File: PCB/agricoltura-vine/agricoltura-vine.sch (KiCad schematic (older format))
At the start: 0 parts

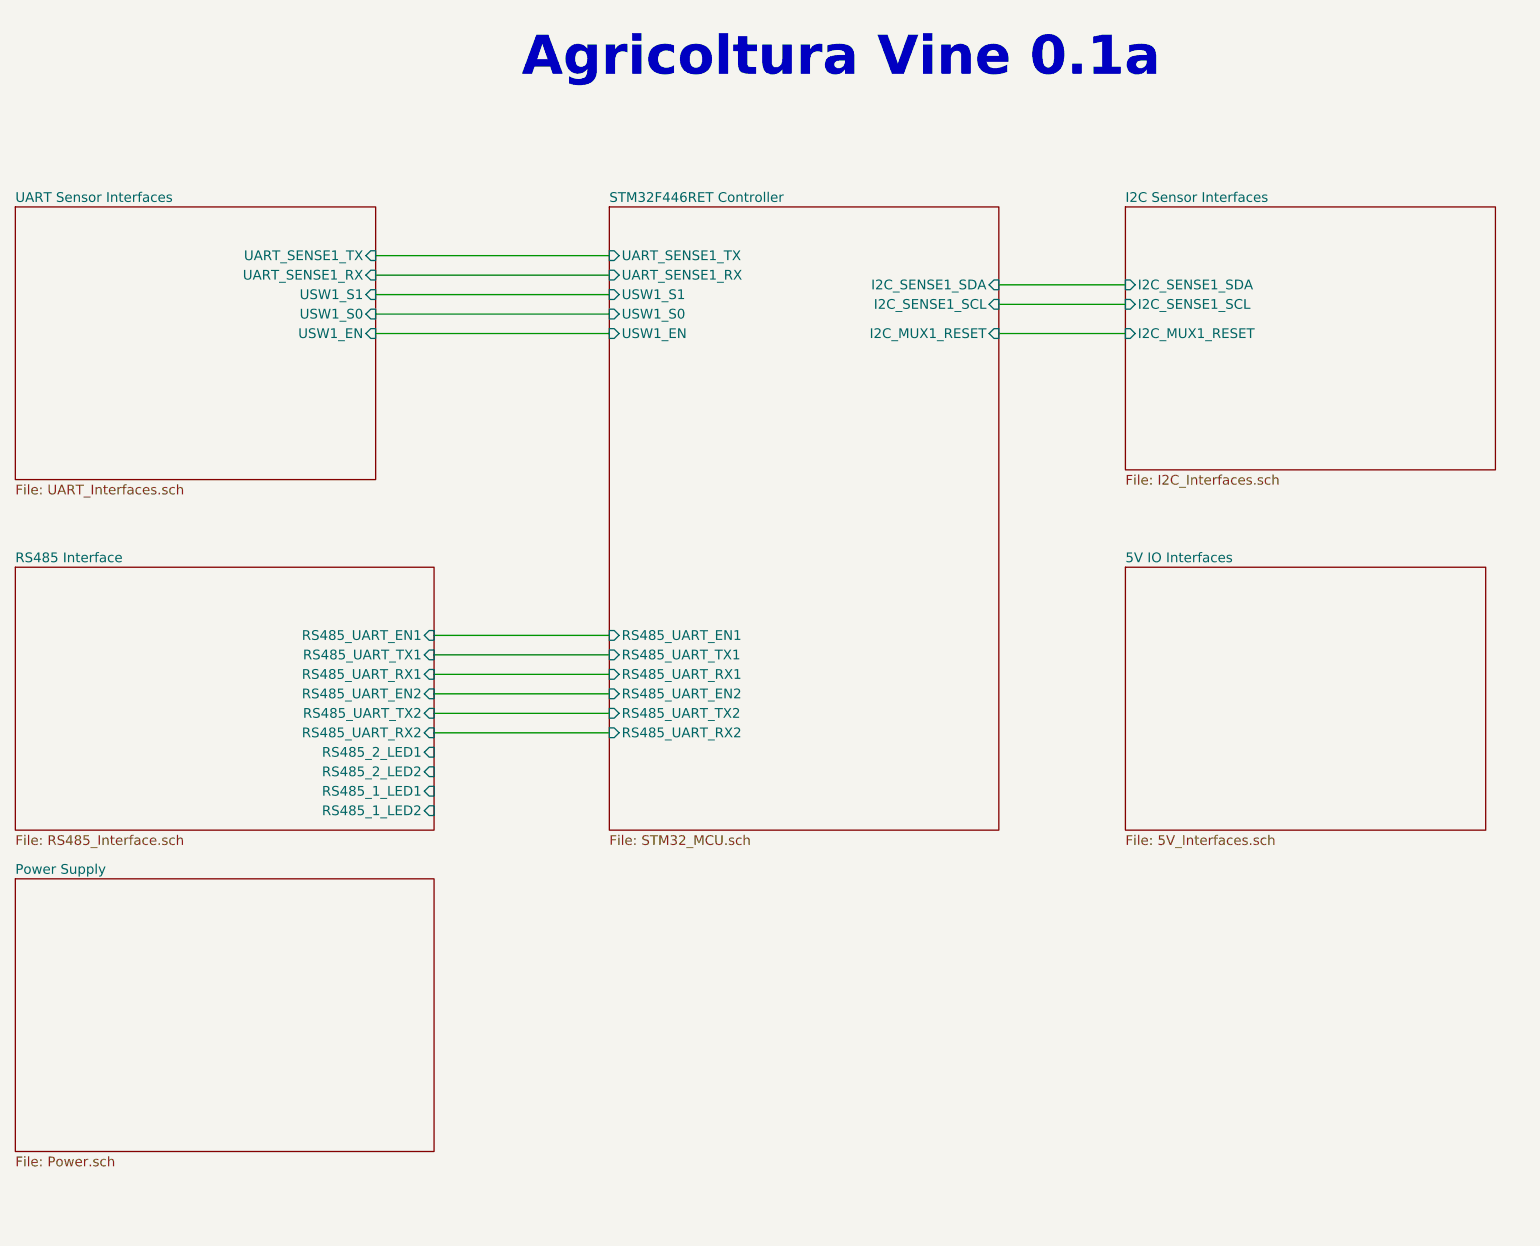
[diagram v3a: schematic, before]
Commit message: Routing and New RS485
swapped over the RS485 chip to a new one and started routing the board.
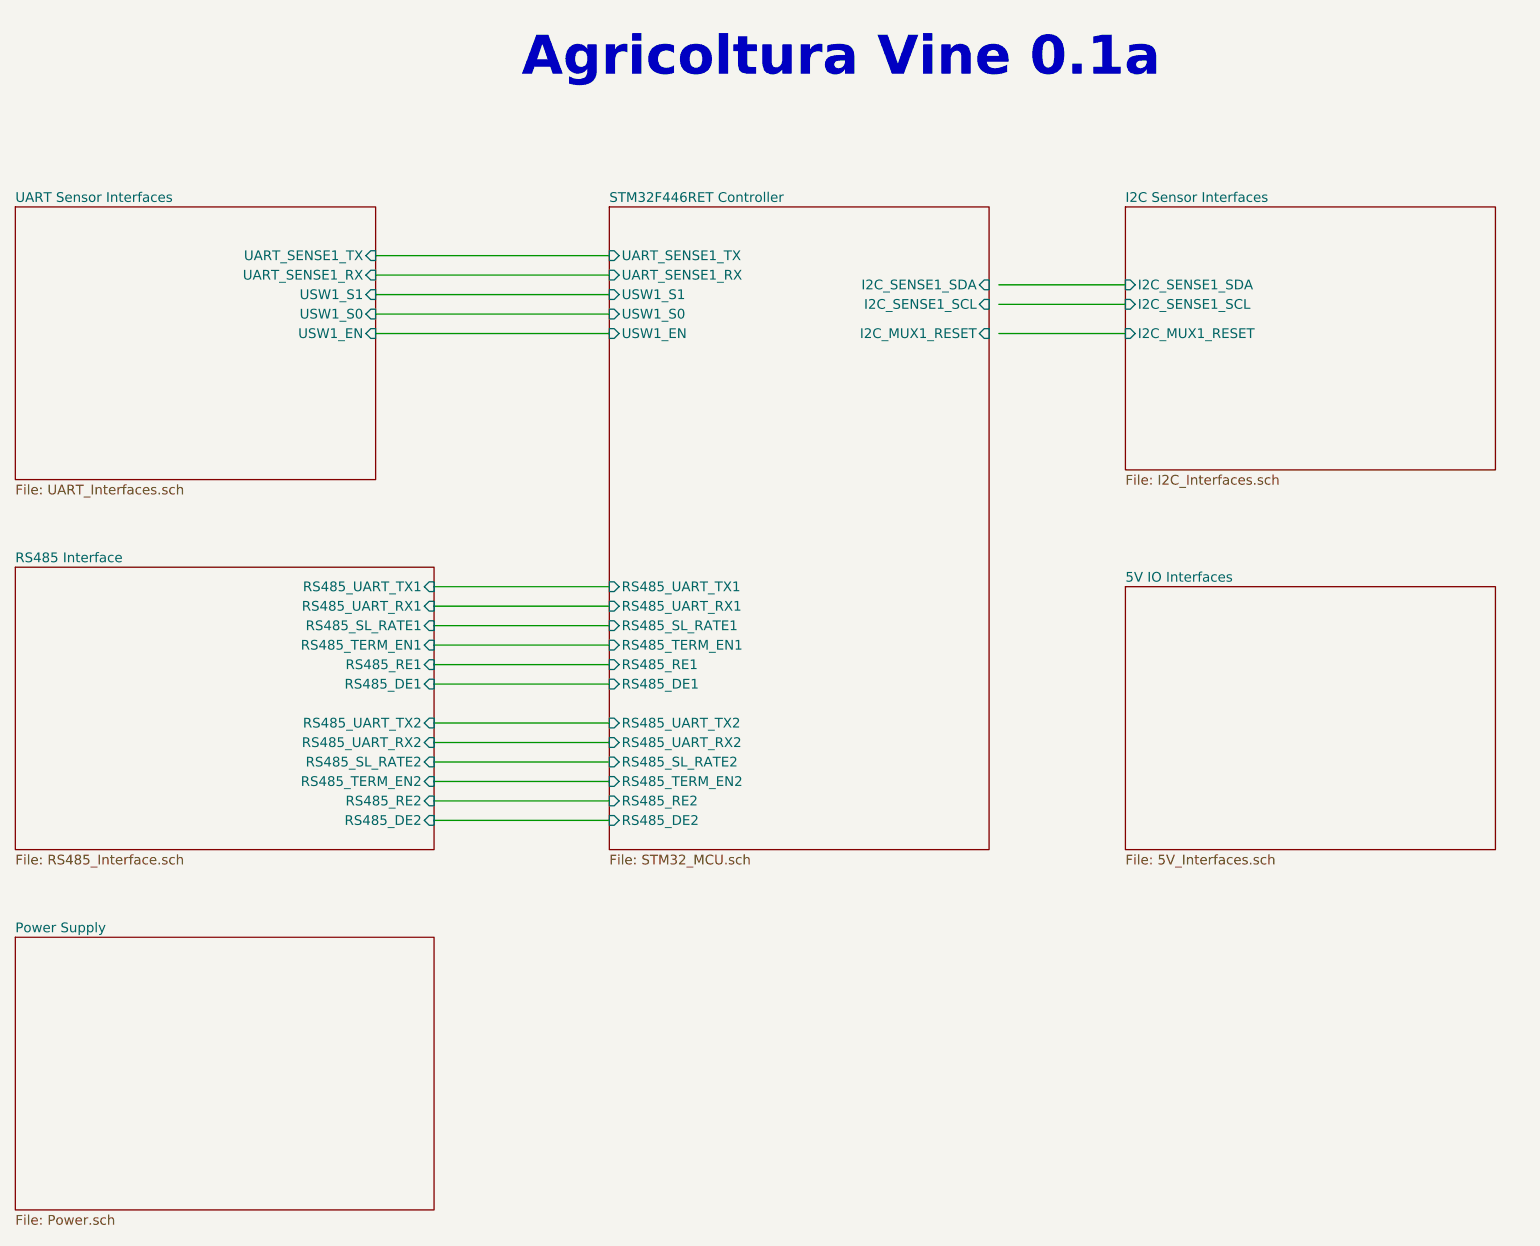
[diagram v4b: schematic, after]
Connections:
- wire segments 14 -> 20
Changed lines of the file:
@@
 $EndDescr
 $Sheet
-S 4700 2000 2000 3200
+S 4700 2000 1950 3300
 U 5EE8264D
 F0 "STM32F446RET Controller" 50
 F1 "STM32_MCU.sch" 50
 F2 "UART_SENSE1_TX" I L 4700 2250 50
-F3 "RS485_UART_EN1" I L 4700 4200 50
-F4 "RS485_UART_TX1" I L 4700 4300 50
-F5 "RS485_UART_RX1" I L 4700 4400 50
-F6 "RS485_UART_EN2" I L 4700 4500 50
-F7 "RS485_UART_TX2" I L 4700 4600 50
-F8 "RS485_UART_RX2" I L 4700 4700 50
-F9 "I2C_SENSE1_SDA" I R 6700 2400 50
-F10 "I2C_SENSE1_SCL" I R 6700 2500 50
-F11 "I2C_MUX1_RESET" I R 6700 2650 50
-F12 "USW1_EN" I L 4700 2650 50
-F13 "USW1_S0" I L 4700 2550 50
-F14 "USW1_S1" I L 4700 2450 50
-F15 "UART_SENSE1_RX" I L 4700 2350 50
+F3 "RS485_UART_TX1" I L 4700 3950 50
+F4 "RS485_UART_RX1" I L 4700 4050 50
+F5 "RS485_UART_TX2" I L 4700 4650 50
+F6 "RS485_UART_RX2" I L 4700 4750 50
+F7 "I2C_SENSE1_SDA" I R 6650 2400 50
+F8 "I2C_SENSE1_SCL" I R 6650 2500 50
+F9 "I2C_MUX1_RESET" I R 6650 2650 50
+F10 "USW1_EN" I L 4700 2650 50
+F11 "USW1_S0" I L 4700 2550 50
+F12 "USW1_S1" I L 4700 2450 50
+F13 "UART_SENSE1_RX" I L 4700 2350 50
+F14 "RS485_DE1" I L 4700 4450 50
+F15 "RS485_DE2" I L 4700 5150 50
+F16 "RS485_TERM_EN1" I L 4700 4250 50
+F17 "RS485_SL_RATE1" I L 4700 4150 50
+F18 "RS485_RE1" I L 4700 4350 50
+F19 "RS485_SL_RATE2" I L 4700 4850 50
+F20 "RS485_RE2" I L 4700 5050 50
+F21 "RS485_TERM_EN2" I L 4700 4950 50
 $EndSheet
 $Sheet
@@
 $EndSheet
 $Sheet
-S 1650 5450 2150 1400
+S 1650 5750 2150 1400
 U 5EE8280D
 F0 "Power Supply" 50
@@
 $EndSheet
 $Sheet
-S 1650 3850 2150 1350
+S 1650 3850 2150 1450
 U 5EE82896
 F0 "RS485 Interface" 50
 F1 "RS485_Interface.sch" 50
-F2 "RS485_UART_EN1" I R 3800 4200 50
-F3 "RS485_UART_TX1" I R 3800 4300 50
-F4 "RS485_UART_RX1" I R 3800 4400 50
-F5 "RS485_UART_EN2" I R 3800 4500 50
-F6 "RS485_UART_TX2" I R 3800 4600 50
-F7 "RS485_UART_RX2" I R 3800 4700 50
-F8 "RS485_2_LED1" I R 3800 4800 50
-F9 "RS485_2_LED2" I R 3800 4900 50
-F10 "RS485_1_LED1" I R 3800 5000 50
-F11 "RS485_1_LED2" I R 3800 5100 50
-$EndSheet
-$Sheet
-S 7350 3850 1850 1350
-U 5EF943A9
-F0 "5V IO Interfaces" 50
-F1 "5V_Interfaces.sch" 50
+F2 "RS485_UART_TX1" I R 3800 3950 50
+F3 "RS485_UART_RX1" I R 3800 4050 50
+F4 "RS485_UART_TX2" I R 3800 4650 50
+F5 "RS485_UART_RX2" I R 3800 4750 50
+F6 "RS485_DE2" I R 3800 5150 50
+F7 "RS485_DE1" I R 3800 4450 50
+F8 "RS485_SL_RATE2" I R 3800 4850 50
+F9 "RS485_SL_RATE1" I R 3800 4150 50
+F10 "RS485_TERM_EN1" I R 3800 4250 50
+F11 "RS485_RE1" I R 3800 4350 50
+F12 "RS485_RE2" I R 3800 5050 50
+F13 "RS485_TERM_EN2" I R 3800 4950 50
 $EndSheet
 Wire Wire Line
-	3800 4200 4700 4200
+	3800 3950 4700 3950
 Wire Wire Line
-	3800 4300 4700 4300
+	4700 4050 3800 4050
 Wire Wire Line
-	4700 4400 3800 4400
+	4700 4650 3800 4650
 Wire Wire Line
-	3800 4500 4700 4500
-Wire Wire Line
-	4700 4600 3800 4600
-Wire Wire Line
-	3800 4700 4700 4700
+	3800 4750 4700 4750
 Wire Wire Line
 	7350 2650 6700 2650
@@
 Text Notes 4250 1350 0    200  ~ 40
 Agricoltura Vine 0.1a
+$Sheet
+S 7350 3950 1900 1350
+U 5EF943A9
+F0 "5V IO Interfaces" 50
+F1 "5V_Interfaces.sch" 50
+$EndSheet
+Wire Wire Line
+	4700 4850 3800 4850
+Wire Wire Line
+	3800 4950 4700 4950
+Wire Wire Line
+	4700 5050 3800 5050
+Wire Wire Line
+	3800 5150 4700 5150
+Wire Wire Line
+	4700 4350 3800 4350
+Wire Wire Line
+	3800 4450 4700 4450
+Wire Wire Line
+	4700 4150 3800 4150
+Wire Wire Line
+	3800 4250 4700 4250
 $EndSCHEMATC

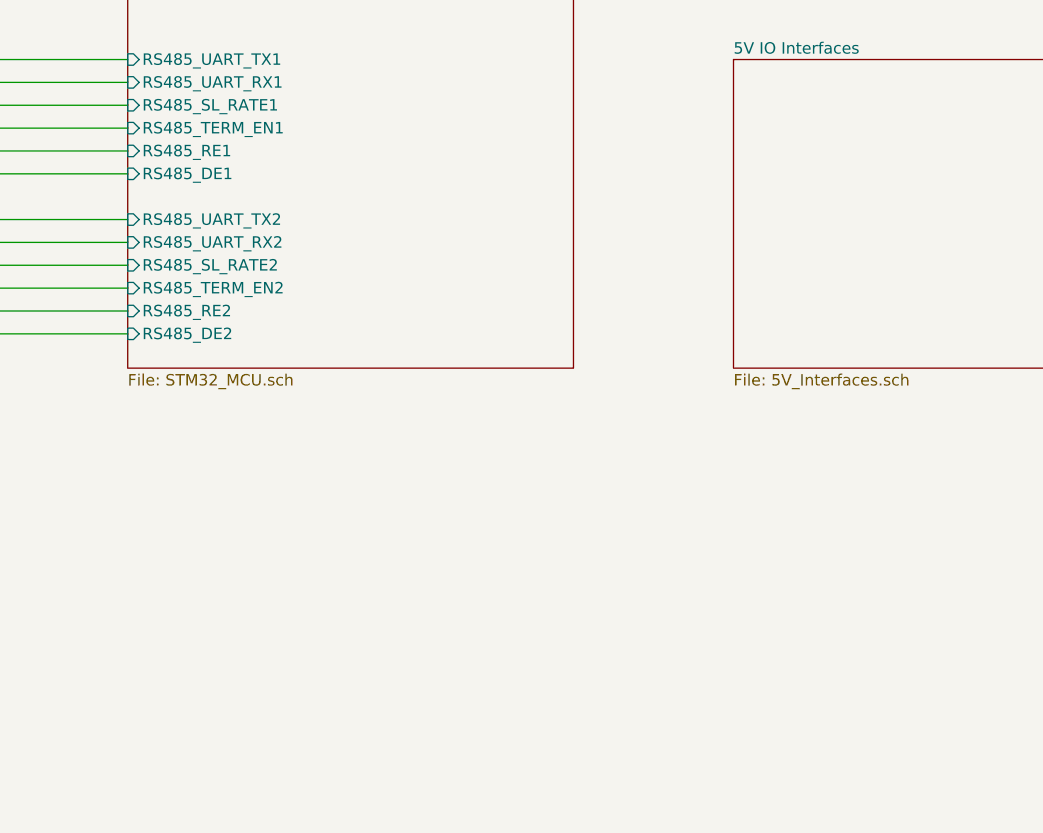
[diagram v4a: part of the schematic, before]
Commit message: Majopr Progress
Board shape enlarged to simplify layout and accomodate larger size parts for sisterboard like Ivy. QWIIC connectors flipped to be correct, signals were oriented incorrectly in past revisions.
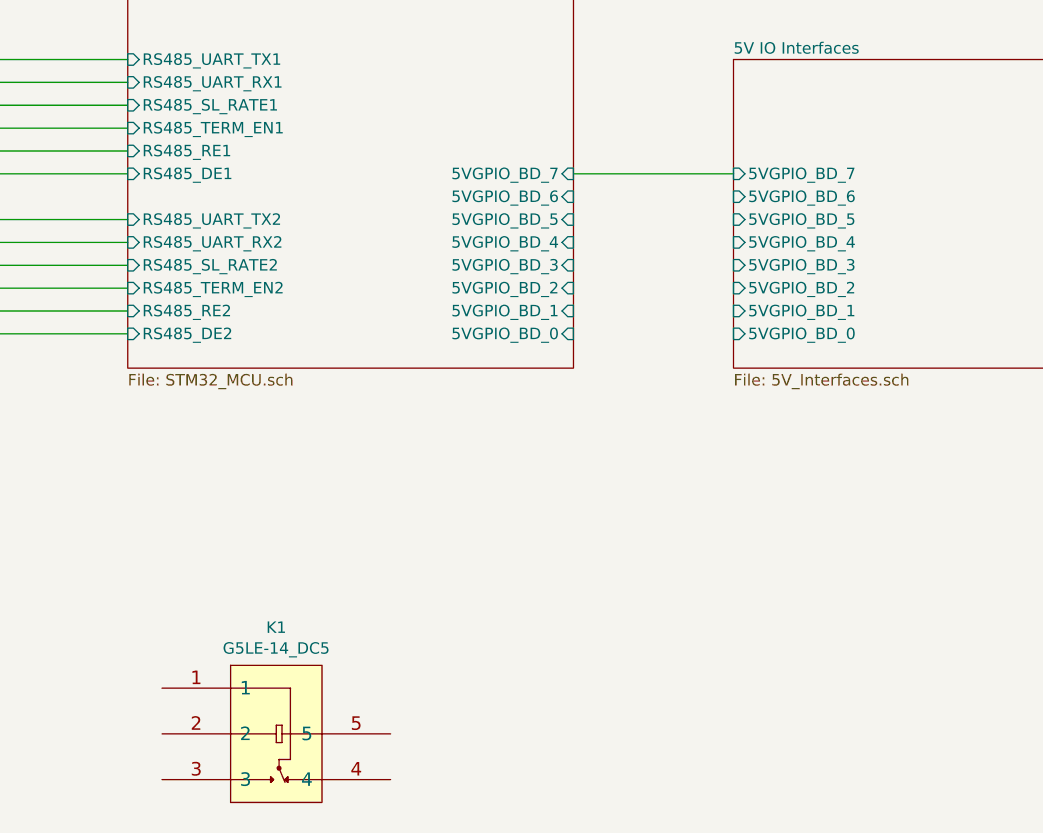
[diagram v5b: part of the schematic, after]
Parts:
- added K1: G5LE-14_DC5, AVR-KiCAD-Lib-Relays-Contactors:G5LE-14_DC5, symbol AVR-KiCAD-Lib-Mech-Relays-Contactors:G5LE-14_DC5
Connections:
- wire segments 20 -> 21
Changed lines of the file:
@@
 F20 "RS485_RE2" I L 4700 5050 50
 F21 "RS485_TERM_EN2" I L 4700 4950 50
+F22 "5VGPIO_BD_0" I R 6650 5150 50
+F23 "5VGPIO_BD_1" I R 6650 5050 50
+F24 "5VGPIO_BD_2" I R 6650 4950 50
+F25 "5VGPIO_BD_3" I R 6650 4850 50
+F26 "5VGPIO_BD_4" I R 6650 4750 50
+F27 "5VGPIO_BD_5" I R 6650 4650 50
+F28 "5VGPIO_BD_6" I R 6650 4550 50
+F29 "5VGPIO_BD_7" I R 6650 4450 50
 $EndSheet
 $Sheet
@@
 F0 "5V IO Interfaces" 50
 F1 "5V_Interfaces.sch" 50
+F2 "5VGPIO_BD_0" I L 7350 5150 50
+F3 "5VGPIO_BD_1" I L 7350 5050 50
+F4 "5VGPIO_BD_2" I L 7350 4950 50
+F5 "5VGPIO_BD_3" I L 7350 4850 50
+F6 "5VGPIO_BD_4" I L 7350 4750 50
+F7 "5VGPIO_BD_5" I L 7350 4650 50
+F8 "5VGPIO_BD_6" I L 7350 4550 50
+F9 "5VGPIO_BD_7" I L 7350 4450 50
 $EndSheet
 Wire Wire Line
@@
 Wire Wire Line
 	3800 4250 4700 4250
+Wire Wire Line
+	6650 4450 7350 4450
+$Comp
+L AVR-KiCAD-Lib-Mech-Relays-Contactors:G5LE-14_DC5 K1
+U 1 1 5F0092A7
+P 5150 6600
+F 0 "K1" H 5350 6765 50  0000 C CNN
+F 1 "G5LE-14_DC5" H 5350 6674 50  0000 C CNN
+F 2 "AVR-KiCAD-Lib-Relays-Contactors:G5LE-14_DC5" H 5150 6600 50  0001 C CNN
+F 3 "https://omronfs.omron.com/en_US/ecb/products/pdf/en-g5le.pdf" H 5150 6600 50  0001 C CNN
+F 4 "1.44000" H 5250 6850 50  0001 C CNN "Cost QTY: 1"
+F 5 "0.84028" H 5350 6950 50  0001 C CNN "Cost QTY: 1000"
+F 6 "*" H 5450 7050 50  0001 C CNN "Cost QTY: 2500"
+F 7 "0.81027" H 5550 7150 50  0001 C CNN "Cost QTY: 5000"
+F 8 "*" H 5650 7250 50  0001 C CNN "Cost QTY: 10000"
+F 9 "Omron Electronics Inc-EMC Div" H 5750 7350 50  0001 C CNN "MFR"
+F 10 "G5LE-14 DC5" H 5850 7450 50  0001 C CNN "MFR#"
+F 11 "Digikey" H 5950 7550 50  0001 C CNN "Vendor"
+F 12 "Z1011-ND" H 6050 7650 50  0001 C CNN "Vendor #"
+F 13 "AVR" H 6150 7750 50  0001 C CNN "Designer"
+F 14 "19mm" H 6250 7850 50  0001 C CNN "Height"
+F 15 "6/23/2020" H 7350 8950 50  0001 C CNN "Date Created"
+F 16 "6/23/2020" H 6350 7950 50  0001 C CNN "Date Modified"
+F 17 "Yes" H 6450 8050 50  0001 C CNN "Lead-Free ?"
+F 18 "1" H 6550 8150 50  0001 C CNN "RoHS Levels"
+F 19 "ThroughHole" H 6650 8250 50  0001 C CNN "Mounting"
+F 20 "5" H 6750 8350 50  0001 C CNN "Pin Count #"
+F 21 "Active" H 6850 8450 50  0001 C CNN "Status"
+F 22 "*" H 6950 8550 50  0001 C CNN "Tolerance"
+F 23 "Relay-Contactor" H 7050 8650 50  0001 C CNN "Type"
+F 24 "5VDC Coil, 250VAC, 125VDC - Max" H 7150 8750 50  0001 C CNN "Voltage"
+F 25 "*" H 7250 8900 50  0001 C CNN "Package"
+F 26 "General Purpose Relay SPDT (1 Form C) 5VDC Coil Through Hole" H 7550 9200 50  0001 C CNN "Description"
+F 27 "G5LE-14 DC5" H 7450 9100 50  0001 C CNN "_Value_"
+F 28 "*" H 7550 9200 50  0001 C CNN "Management_ID"
+	1    5150 6600
+	1    0    0    -1
+$EndComp
 $EndSCHEMATC

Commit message: IO Expander
added IO expander for 5V IOs
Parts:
- removed K1: G5LE-14_DC5, AVR-KiCAD-Lib-Relays-Contactors:G5LE-14_DC5, symbol AVR-KiCAD-Lib-Mech-Relays-Contactors:G5LE-14_DC5
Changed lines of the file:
@@
 Wire Wire Line
 	6650 4450 7350 4450
-$Comp
-L AVR-KiCAD-Lib-Mech-Relays-Contactors:G5LE-14_DC5 K1
-U 1 1 5F0092A7
-P 5150 6600
-F 0 "K1" H 5350 6765 50  0000 C CNN
-F 1 "G5LE-14_DC5" H 5350 6674 50  0000 C CNN
-F 2 "AVR-KiCAD-Lib-Relays-Contactors:G5LE-14_DC5" H 5150 6600 50  0001 C CNN
-F 3 "https://omronfs.omron.com/en_US/ecb/products/pdf/en-g5le.pdf" H 5150 6600 50  0001 C CNN
-F 4 "1.44000" H 5250 6850 50  0001 C CNN "Cost QTY: 1"
-F 5 "0.84028" H 5350 6950 50  0001 C CNN "Cost QTY: 1000"
-F 6 "*" H 5450 7050 50  0001 C CNN "Cost QTY: 2500"
-F 7 "0.81027" H 5550 7150 50  0001 C CNN "Cost QTY: 5000"
-F 8 "*" H 5650 7250 50  0001 C CNN "Cost QTY: 10000"
-F 9 "Omron Electronics Inc-EMC Div" H 5750 7350 50  0001 C CNN "MFR"
-F 10 "G5LE-14 DC5" H 5850 7450 50  0001 C CNN "MFR#"
-F 11 "Digikey" H 5950 7550 50  0001 C CNN "Vendor"
-F 12 "Z1011-ND" H 6050 7650 50  0001 C CNN "Vendor #"
-F 13 "AVR" H 6150 7750 50  0001 C CNN "Designer"
-F 14 "19mm" H 6250 7850 50  0001 C CNN "Height"
-F 15 "6/23/2020" H 7350 8950 50  0001 C CNN "Date Created"
-F 16 "6/23/2020" H 6350 7950 50  0001 C CNN "Date Modified"
-F 17 "Yes" H 6450 8050 50  0001 C CNN "Lead-Free ?"
-F 18 "1" H 6550 8150 50  0001 C CNN "RoHS Levels"
-F 19 "ThroughHole" H 6650 8250 50  0001 C CNN "Mounting"
-F 20 "5" H 6750 8350 50  0001 C CNN "Pin Count #"
-F 21 "Active" H 6850 8450 50  0001 C CNN "Status"
-F 22 "*" H 6950 8550 50  0001 C CNN "Tolerance"
-F 23 "Relay-Contactor" H 7050 8650 50  0001 C CNN "Type"
-F 24 "5VDC Coil, 250VAC, 125VDC - Max" H 7150 8750 50  0001 C CNN "Voltage"
-F 25 "*" H 7250 8900 50  0001 C CNN "Package"
-F 26 "General Purpose Relay SPDT (1 Form C) 5VDC Coil Through Hole" H 7550 9200 50  0001 C CNN "Description"
-F 27 "G5LE-14 DC5" H 7450 9100 50  0001 C CNN "_Value_"
-F 28 "*" H 7550 9200 50  0001 C CNN "Management_ID"
-	1    5150 6600
-	1    0    0    -1
-$EndComp
 $EndSCHEMATC
